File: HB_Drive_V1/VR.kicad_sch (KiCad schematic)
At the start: 48 parts, among them J201 Conn_02x02_Odd_Even, J202 Conn_02x03_Odd_Even, J203 Conn_01x03, U201 TL082, U202 TL082, U203 TL082, U204 TL082, U205 TL082

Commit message: Brings everything up to latest copy on my computer
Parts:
- added TP208, TP209: TestPoint, TestPoint:TestPoint_Loop_D2.60mm_Drill1.6mm_Beaded, symbol Connector:TestPoint
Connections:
- net -Int_Reg_Cmd: now also TP209.1
- net -Prop_Reg_Cmd: now also TP208.1
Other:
- company: (none) -> UW Madison, WEMPEC
- title: (none) -> HB Drive V3
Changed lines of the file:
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@@
 	(generator_version "10.0")
 	(paper "A3")
+	(title_block
+		(title "HB Drive V3")
+		(date "2026-09-08")
+		(company "UW Madison, WEMPEC")
+	)
 	(rectangle
 		(start 76.2 59.69)
@@
 	)
 	(junction
+		(at 317.5 113.03)
+		(diameter 0)
+		(color 0 0 0 0)
+	)
+	(junction
 		(at 184.15 69.85)
 		(diameter 0)
@@
 	)
 	(junction
+		(at 298.45 81.28)
+		(diameter 0)
+		(color 0 0 0 0)
+	)
+	(junction
 		(at 204.47 87.63)
 		(diameter 0)
@@
 	(wire
 		(pts
-			(xy 289.56 81.28) (xy 307.34 81.28)
+			(xy 289.56 81.28) (xy 298.45 81.28)
 		)
 		(stroke
@@
 	(wire
 		(pts
-			(xy 307.34 113.03) (xy 323.85 113.03)
+			(xy 307.34 113.03) (xy 317.5 113.03)
 		)
 		(stroke
@@
 	(wire
 		(pts
+			(xy 298.45 81.28) (xy 307.34 81.28)
+		)
+		(stroke
+			(width 0)
+			(type default)
+		)
+	)
+	(wire
+		(pts
 			(xy 154.94 171.45) (xy 157.48 171.45)
 		)
@@
 	(wire
 		(pts
+			(xy 317.5 113.03) (xy 323.85 113.03)
+		)
+		(stroke
+			(width 0)
+			(type default)
+		)
+	)
+	(wire
+		(pts
 			(xy 134.62 123.19) (xy 142.24 123.19)
 		)
@@
 	)
 	(symbol
+		(lib_id "Connector:TestPoint")
+		(at 317.5 113.03 180)
+		(unit 1)
+		(body_style 1)
+		(exclude_from_sim no)
+		(in_bom yes)
+		(on_board yes)
+		(in_pos_files yes)
+		(dnp no)
+		(property "Reference" "TP209"
+			(at 317.246 117.856 0)
+			(show_name no)
+			(do_not_autoplace no)
+			(effects
+				(font
+					(size 1.27 1.27)
+				)
+				(justify left)
+			)
+		)
+		(property "Value" "TestPoint"
+			(at 314.96 115.0621 0)
+			(hide yes)
+			(show_name no)
+			(do_not_autoplace no)
+			(effects
+				(font
+					(size 1.27 1.27)
+				)
+				(justify left)
+			)
+		)
+		(property "Footprint" "TestPoint:TestPoint_Loop_D2.60mm_Drill1.6mm_Beaded"
+			(at 312.42 113.03 0)
+			(hide yes)
+			(show_name no)
+			(do_not_autoplace no)
+			(effects
+				(font
+					(size 1.27 1.27)
+				)
+			)
+		)
+		(property "Datasheet" ""
+			(at 312.42 113.03 0)
+			(hide yes)
+			(show_name no)
+			(do_not_autoplace no)
+			(effects
+				(font
+					(size 1.27 1.27)
+				)
+			)
+		)
+		(property "Description" "test point"
+			(at 317.5 113.03 0)
+			(hide yes)
+			(show_name no)
+			(do_not_autoplace no)
+			(effects
+				(font
+					(size 1.27 1.27)
+				)
+			)
+		)
+		(property "Sim.Device" ""
+			(at 317.5 113.03 90)
+			(hide yes)
+			(show_name no)
+			(do_not_autoplace no)
+			(effects
+				(font
+					(size 1.27 1.27)
+				)
+			)
+		)
+		(pin "1"
+		)
+		(instances
+			(project "HB_Drive_V1"
+				(path "/a9b54c89-4c8e-4c90-8a0d-ec2009e369b7/cbb6a335-cf9f-454a-a7da-871f74bddb32"
+					(reference "TP209")
+					(unit 1)
+				)
+			)
+		)
+	)
+	(symbol
 		(lib_id "Connector_Generic:Conn_02x03_Odd_Even")
 		(at 100.33 130.81 0)
@@
 					(unit 1)
 				)
+			)
+		)
+	)
+	(symbol
+		(lib_id "Connector:TestPoint")
+		(at 298.45 81.28 180)
+		(unit 1)
+		(body_style 1)
+		(exclude_from_sim no)
+		(in_bom yes)
+		(on_board yes)
+		(in_pos_files yes)
+		(dnp no)
+		(property "Reference" "TP208"
+			(at 298.196 86.106 0)
+			(show_name no)
+			(do_not_autoplace no)
+			(effects
+				(font
+					(size 1.27 1.27)
+				)
+				(justify left)
+			)
+		)
+		(property "Value" "TestPoint"
+			(at 295.91 83.3121 0)
+			(hide yes)
+			(show_name no)
+			(do_not_autoplace no)
+			(effects
+				(font
+					(size 1.27 1.27)
+				)
+				(justify left)
+			)
+		)
+		(property "Footprint" "TestPoint:TestPoint_Loop_D2.60mm_Drill1.6mm_Beaded"
+			(at 293.37 81.28 0)
+			(hide yes)
+			(show_name no)
+			(do_not_autoplace no)
+			(effects
+				(font
+					(size 1.27 1.27)
+				)
+			)
+		)
+		(property "Datasheet" ""
+			(at 293.37 81.28 0)
+			(hide yes)
+			(show_name no)
+			(do_not_autoplace no)
+			(effects
+				(font
+					(size 1.27 1.27)
+				)
+			)
+		)
+		(property "Description" "test point"
+			(at 298.45 81.28 0)
+			(hide yes)
+			(show_name no)
+			(do_not_autoplace no)
+			(effects
+				(font
+					(size 1.27 1.27)
+				)
+			)
+		)
+		(property "Sim.Device" ""
+			(at 298.45 81.28 90)
+			(hide yes)
+			(show_name no)
+			(do_not_autoplace no)
+			(effects
+				(font
+					(size 1.27 1.27)
+				)
+			)
+		)
+		(pin "1"
+		)
+		(instances
+			(project "HB_Drive_V1"
+				(path "/a9b54c89-4c8e-4c90-8a0d-ec2009e369b7/cbb6a335-cf9f-454a-a7da-871f74bddb32"
+					(reference "TP208")
+					(unit 1)
+				)

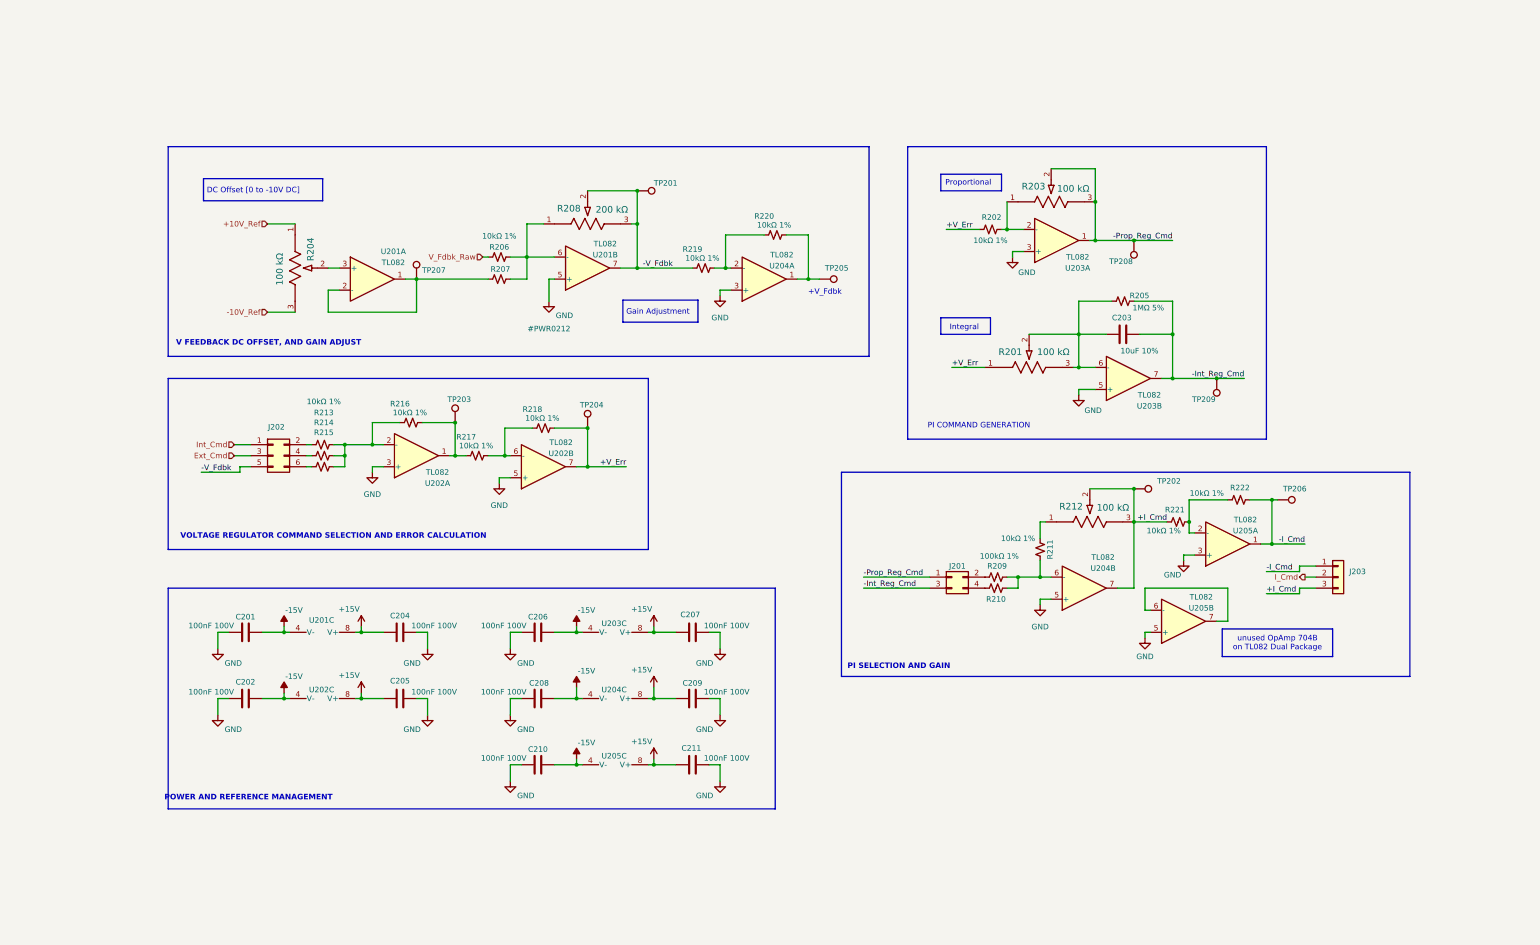
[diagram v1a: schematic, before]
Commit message: Makes annotation changes
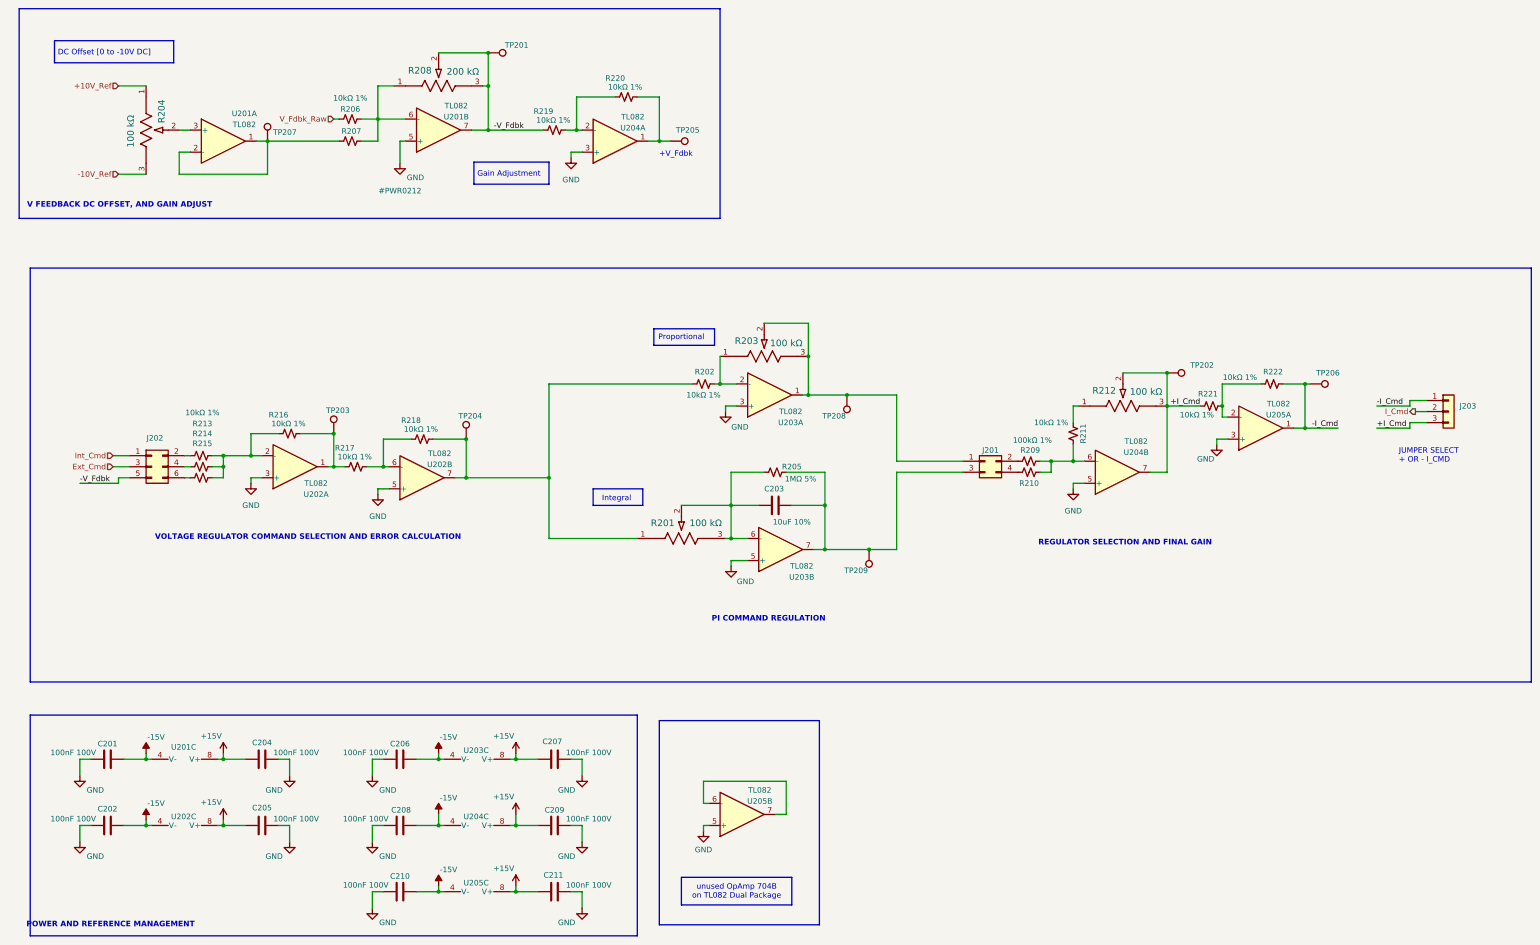
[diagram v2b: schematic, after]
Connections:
- net +V_Err: no longer names the net of R201.1, R202.1, R218.1, TP204.1, U202.7
- net -Int_Reg_Cmd: no longer names the net of C203.1, J201.3 (Pin_3), R205.2, TP209.1, U203.7
- net -Prop_Reg_Cmd: no longer names the net of J201.1 (Pin_1), R203.2, R203.3, TP208.1, U203.1
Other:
- note added: "JUMPER SELECT + OR - I_CMD"
- note added: "PI COMMAND REGULATION"
- note added: "REGULATOR SELECTION AND FINAL GAIN"
- note removed: "PI COMMAND GENERATION"
- note removed: "PI SELECTION AND GAIN"
- moved on the sheet: C201, C202, C203, C204, C205, C206, C207, C208, C209, C210, C211, J201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
